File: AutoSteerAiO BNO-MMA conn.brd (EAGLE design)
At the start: 114.3 x 99.1 mm, 84 parts, among them J4 CONNECTOR 1x5 PINS, K4 CB1A-P-12V, U1 VX7805-1000

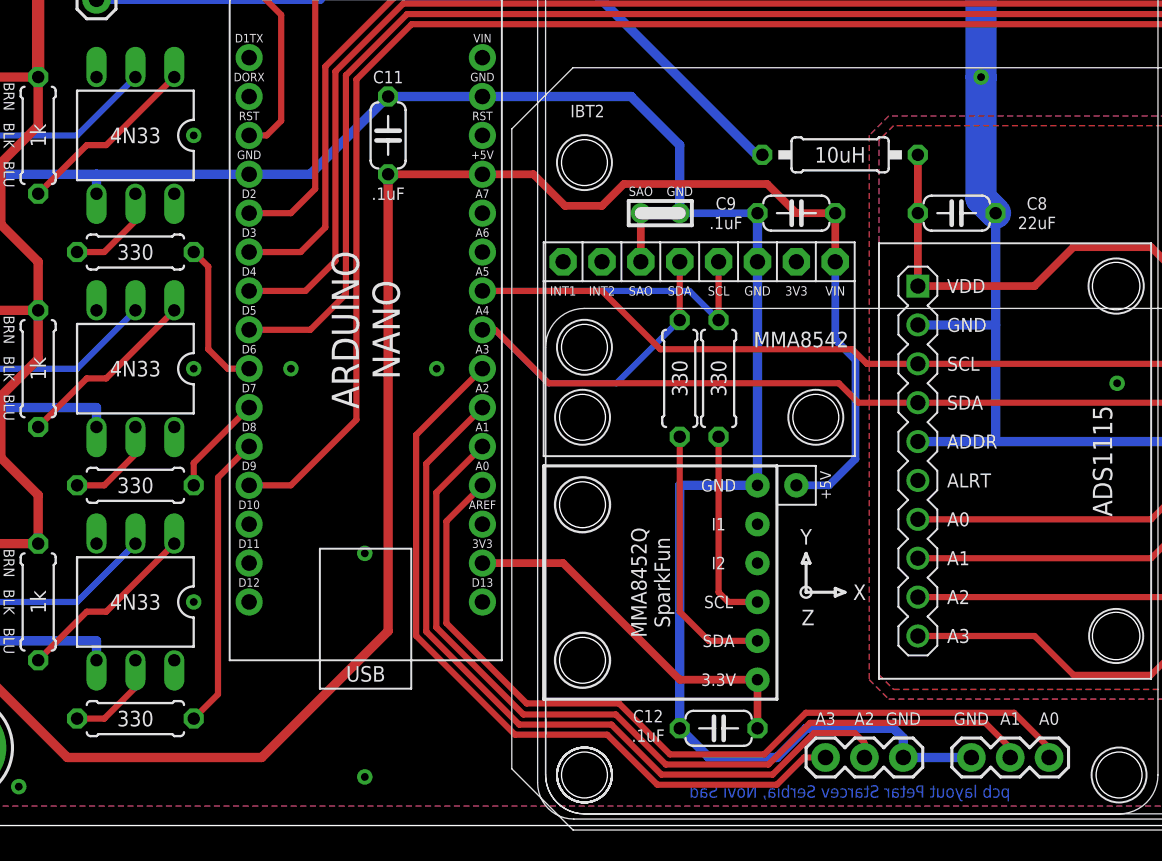
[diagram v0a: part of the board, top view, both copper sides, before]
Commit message: Add files via upload
Added a connector for BNO and MMA
you can use the adapters to place the sensors out of the board
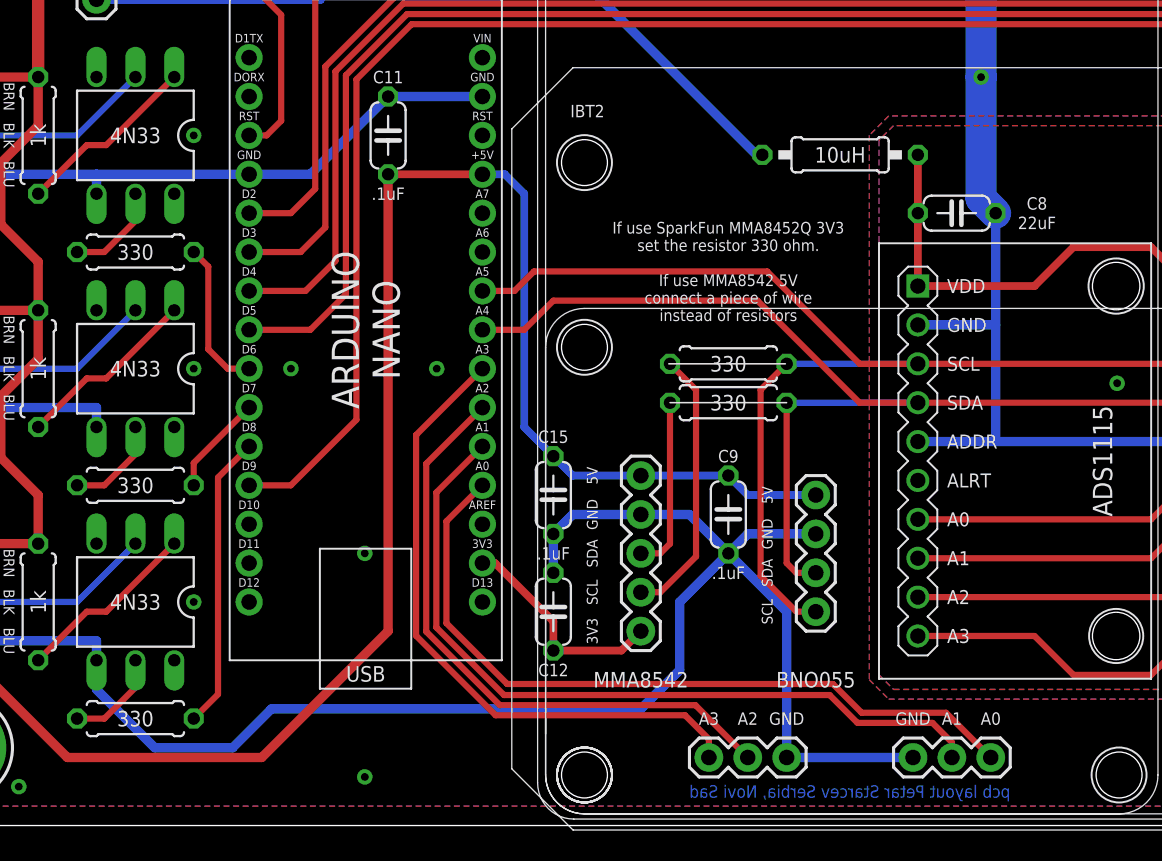
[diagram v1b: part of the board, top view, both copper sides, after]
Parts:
- removed MMA8542: MMA8542, #MMA8542:MMA8452
- removed U$13: MMA8542Q, #MMA8542Q:MMA8542Q
- added C15: .1uF, resistor:C050-024X044
- added J1: (no value), SparkFun-Connectors:1X04
- added J2: (no value), SparkFun-Connectors:1X05
- moved C9 20.2 mm to (55.2, 20.3), turned to 90 degrees
- moved C12 13.2 mm to (43.8, 14.0), turned to 270 degrees
- moved 0 7.62 mm to (54.0, 4.45)
- moved 1 3.81 mm to (67.3, 4.45)
- moved R6 3.55 mm to (55.2, 27.6), turned to 0 degrees
- moved R7 1.14 mm to (55.2, 30.2), turned to 0 degrees
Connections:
- removed net SAO: MMA8542.SAO
- net +3V3: now also J2.5; no longer U$13.3V3
- net +5V: now also C15.2, J1.1, J2.1; no longer MMA8542.VIN
- net GND: now also C15.1, J1.2, J2.2; no longer MMA8542.GND, U$13.GND
- net N$1: now also J2.3; no longer U$13.SDA
- net N$9: now also J2.4; no longer U$13.SCL
- net SCL: now also J1.4; no longer MMA8542.SCL
- net SDA: now also J1.3; no longer MMA8542.SDA
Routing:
- net GND: track 586.4 -> 599.4 mm, vias 70 -> 69
- net A2: track 51.0 -> 40.6 mm
- net +3V3: track 24.3 -> 14.4 mm
- net SCL: track 98.1 -> 106.8 mm
- net A3: track 50.8 -> 42.4 mm
- net +5V: track 245.5 -> 238.4 mm, vias 1 -> 0
- net A0: track 55.6 -> 49.2 mm
- net N$1: track 17.3 -> 11.4 mm
- net A1: track 56.7 -> 50.8 mm
- net N$9: track 13.0 -> 17.9 mm
- net SAO: track 3.18 -> 0.00 mm, vias 1 -> 0
- net SDA: track 97.9 -> 100.8 mm
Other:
- board text added: "3V3"
- board text added: "BNO055"
- board text added: "If use SparkFun MMA8452Q 3V3 set the resistor 330 ohm. If use MMA8542 5V connect a piece of wire instead of resistors"
- board text removed: "MMA8452"
- board text removed: "MMA8452Q"
- board text removed: "SAO"
- board text removed: "X"
- board text removed: "Y"
- board text removed: "Z"
